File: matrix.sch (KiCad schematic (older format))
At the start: 134 parts, among them SW1 SW_Push, SW10 SW_Push, SW11 SW_Push, SW12 SW_Push, SW13 SW_Push, SW14 SW_Push, SW15 SW_Push, SW16 SW_Push, SW17 SW_Push, SW18 SW_Push, SW19 SW_Push, SW2 SW_Push, SW20 SW_Push, SW21 SW_Push, SW22 SW_Push, SW23 SW_Push, SW24 SW_Push, SW25 SW_Push, SW26 SW_Push, SW27 SW_Push, SW28 SW_Push, SW29 SW_Push, SW3 SW_Push, SW30 SW_Push, SW31 SW_Push, SW32 SW_Push, SW33 SW_Push, SW34 SW_Push, SW35 SW_Push, SW36 SW_Push, SW37 SW_Push, SW38 SW_Push, SW39 SW_Push, SW4 SW_Push, SW40 SW_Push, SW41 SW_Push, SW42 SW_Push, SW43 SW_Push, SW44 SW_Push, SW45 SW_Push, SW46 SW_Push, SW47 SW_Push, SW48 SW_Push, SW49 SW_Push, SW5 SW_Push, SW50 SW_Push, SW51 SW_Push, SW52 SW_Push, SW53 SW_Push, SW54 SW_Push, SW55 SW_Push, SW56 SW_Push, SW57 SW_Push, SW58 SW_Push, SW59 SW_Push, SW6 SW_Push, SW60 SW_Push, SW61 SW_Push, SW62 SW_Push, SW63 SW_Push, SW64 SW_Push, SW65 SW_Push, SW66 SW_Push, SW67 SW_Push, SW7 SW_Push, SW8 SW_Push, SW9 SW_Push

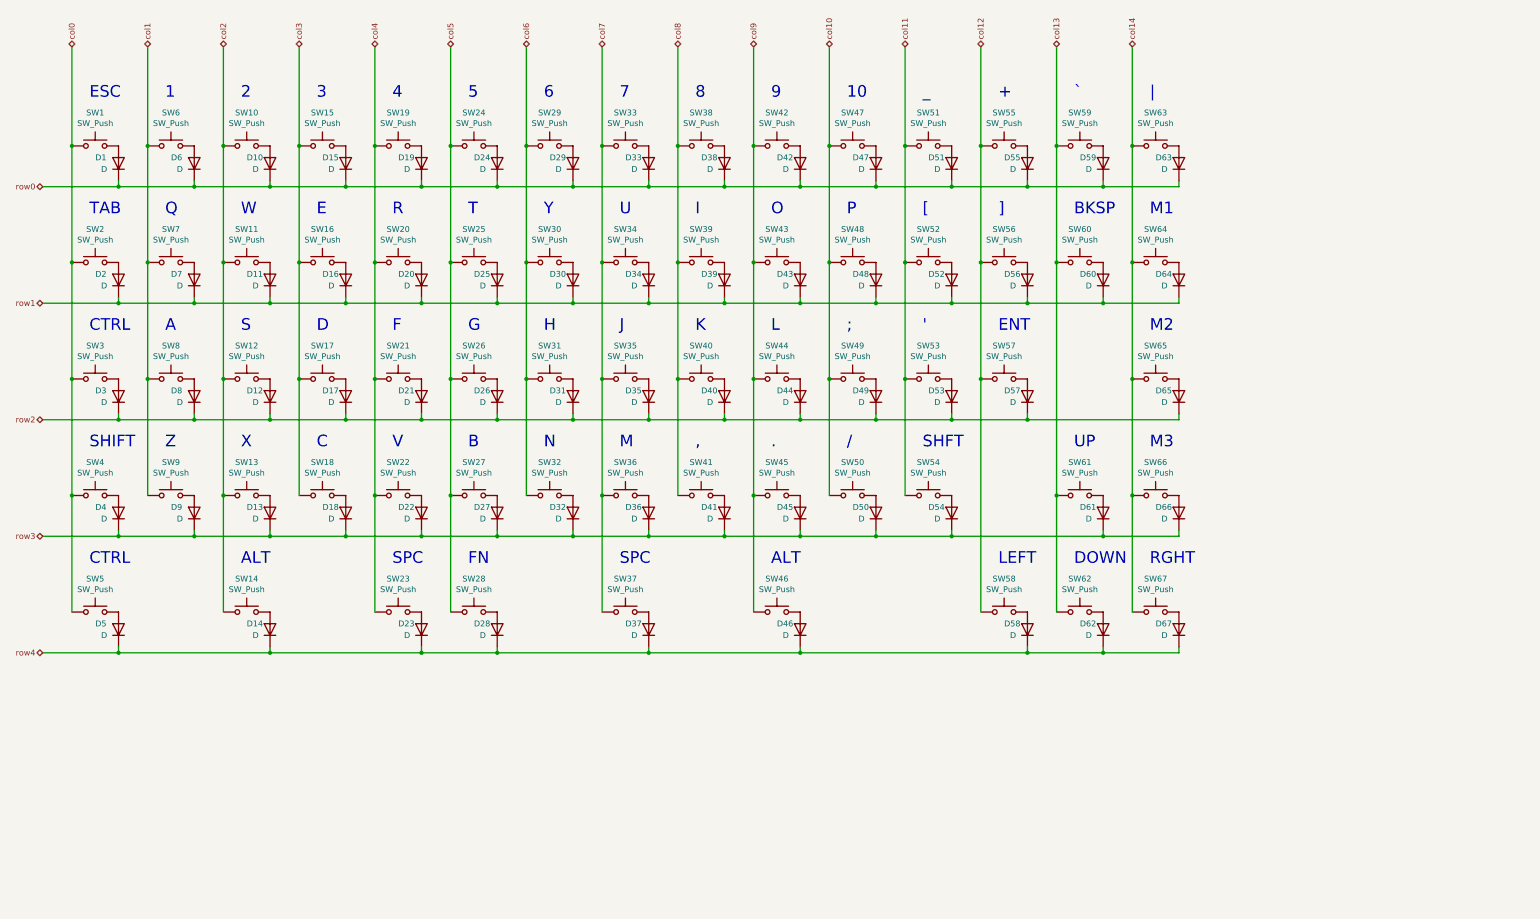
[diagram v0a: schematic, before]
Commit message: USB-C, hotswaps, ESD update, plates, so much
Added USB-C, updated case files, ESD rework, FR4 plates made, name change, hotswap sockets, route rework
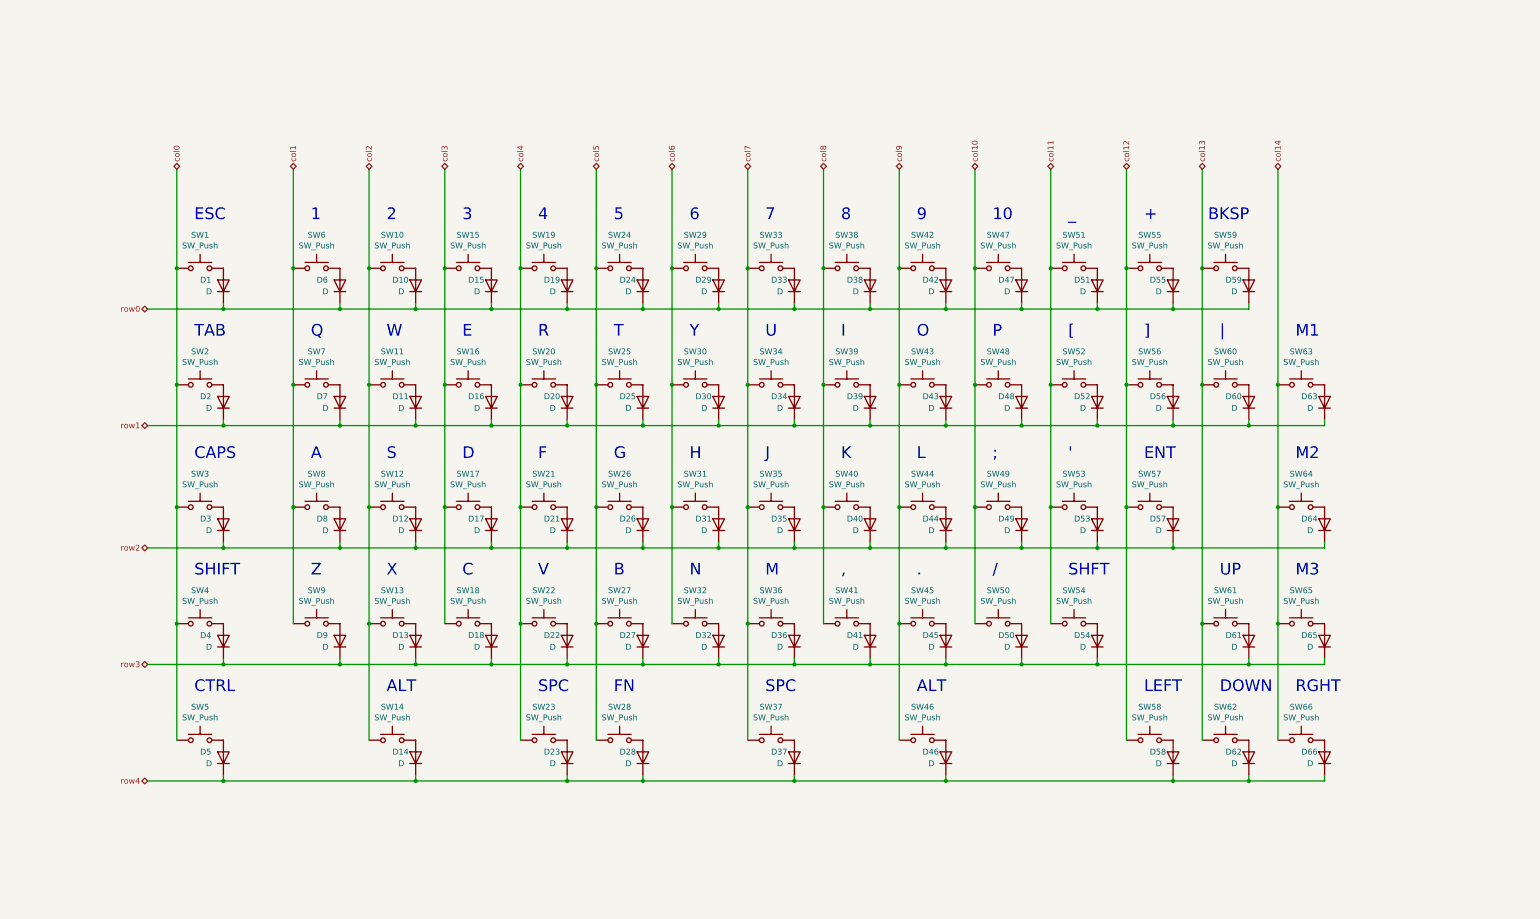
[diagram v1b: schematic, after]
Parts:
- removed D63: D, Diodes_SMD:D_SOD-123, symbol Device:D
- removed SW63: SW_Push, MX_Switch:SW_Cherry_MX_1.00u_PCB, symbol Switch:SW_Push
- D1, D10, D11, D12, D13, D14, D15, D16, D17, D18, D19, D2, D20, D21, D22, D23, D24, D25, D26, D27, D28, D29, D3, D30, D31, D32, D33, D34, D35, D36, D37, D38, D39, D4, D40, D41, D42, D43, D44, D45, D46, D47, D48, D49, D5, D50, D51, D52, D53, D54, D55, D56, D57, D58, D59, D6, D60, D61, D62, D7, D8, D9: footprint Diodes_SMD:D_SOD-123 -> Diode_SMD:D_SOD-123; LCSC (none) -> C81598
- D63: renamed from D64; footprint Diodes_SMD:D_SOD-123 -> Diode_SMD:D_SOD-123; LCSC (none) -> C81598
- D64: renamed from D65; footprint Diodes_SMD:D_SOD-123 -> Diode_SMD:D_SOD-123; LCSC (none) -> C81598
- D65: renamed from D66; footprint Diodes_SMD:D_SOD-123 -> Diode_SMD:D_SOD-123; LCSC (none) -> C81598
- D66: renamed from D67; footprint Diodes_SMD:D_SOD-123 -> Diode_SMD:D_SOD-123; LCSC (none) -> C81598
- SW1, SW10, SW11, SW12, SW13, SW15, SW16, SW17, SW18, SW19, SW20, SW21, SW22, SW24, SW25, SW26, SW27, SW28, SW29, SW30, SW31, SW32, SW33, SW34, SW35, SW36, SW38, SW39, SW40, SW41, SW42, SW43, SW44, SW45, SW47, SW48, SW49, SW50, SW51, SW52, SW53, SW55, SW56, SW58, SW6, SW61, SW62, SW7, SW8, SW9: footprint MX_Switch:SW_Cherry_MX_1.00u_PCB -> arisutea:SW_Hotswap_Kailh_1.00u
- SW14, SW46: footprint MX_Switch:SW_Cherry_MX_1.50u_PCB -> arisutea:SW_Hotswap_Kailh_1.00u
- SW2, SW5, SW60: footprint MX_Switch:SW_Cherry_MX_1.50u_PCB -> arisutea:SW_Hotswap_Kailh_1.50u
- SW23: footprint MX_Switch:SW_Cherry_MX_2.00u_PCB_ReversedStabilizers -> arisutea:SW_Hotswap_Kailh_2.00u_RevStab
- SW3, SW54: footprint MX_Switch:SW_Cherry_MX_1.75u_PCB -> arisutea:SW_Hotswap_Kailh_1.75u
- SW37: footprint MX_Switch:SW_Cherry_MX_2.75u_PCB_ReversedStabilizers -> arisutea:SW_Hotswap_Kailh_2.75u_RevStab
- SW4: footprint MX_Switch:SW_Cherry_MX_2.25u_PCB -> arisutea:SW_Hotswap_Kailh_2.25u
- SW57: footprint MX_Switch:SW_Cherry_MX_2.25u_PCB_ReversedStabilizers -> arisutea:SW_Hotswap_Kailh_2.25u_RevStab
- SW59: footprint MX_Switch:SW_Cherry_MX_1.00u_PCB -> arisutea:SW_Hotswap_Kailh_2.00u
- SW63: renamed from SW64; footprint MX_Switch:SW_Cherry_MX_1.00u_PCB -> arisutea:SW_Hotswap_Kailh_1.00u
- SW64: renamed from SW65; footprint MX_Switch:SW_Cherry_MX_1.00u_PCB -> arisutea:SW_Hotswap_Kailh_1.00u
- SW65: renamed from SW66; footprint MX_Switch:SW_Cherry_MX_1.00u_PCB -> arisutea:SW_Hotswap_Kailh_1.00u
- SW66: renamed from SW67; footprint MX_Switch:SW_Cherry_MX_1.00u_PCB -> arisutea:SW_Hotswap_Kailh_1.00u
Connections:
- net col0: now also SW1.2, SW2.2, SW3.2, SW4.2, SW5.2; no longer SW1.1, SW2.1, SW3.1, SW4.1, SW5.1
- net col1: now also SW6.2, SW7.2, SW8.2, SW9.2; no longer SW6.1, SW7.1, SW8.1, SW9.1
- net col10: now also SW47.2, SW48.2, SW49.2, SW50.2; no longer SW47.1, SW48.1, SW49.1, SW50.1
- net col11: now also SW51.2, SW52.2, SW53.2, SW54.2; no longer SW51.1, SW52.1, SW53.1, SW54.1
- net col12: now also SW55.2, SW56.2, SW57.2, SW58.2; no longer SW55.1, SW56.1, SW57.1, SW58.1
- net col13: now also SW59.2, SW60.2, SW61.2, SW62.2; no longer SW59.1, SW60.1, SW61.1, SW62.1
- net col14: now also SW63.2, SW64.2, SW65.2, SW66.2; no longer SW63.1, SW64.1, SW65.1, SW66.1
- net col2: now also SW10.2, SW11.2, SW12.2, SW13.2, SW14.2; no longer SW10.1, SW11.1, SW12.1, SW13.1, SW14.1
- net col3: now also SW15.2, SW16.2, SW17.2, SW18.2; no longer SW15.1, SW16.1, SW17.1, SW18.1
- net col4: now also SW19.2, SW20.2, SW21.2, SW22.2, SW23.2; no longer SW19.1, SW20.1, SW21.1, SW22.1, SW23.1
- net col5: now also SW24.2, SW25.2, SW26.2, SW27.2, SW28.2; no longer SW24.1, SW25.1, SW26.1, SW27.1, SW28.1
- net col6: now also SW29.2, SW30.2, SW31.2, SW32.2; no longer SW29.1, SW30.1, SW31.1, SW32.1
- net col7: now also SW33.2, SW34.2, SW35.2, SW36.2, SW37.2; no longer SW33.1, SW34.1, SW35.1, SW36.1, SW37.1
- net col8: now also SW38.2, SW39.2, SW40.2, SW41.2; no longer SW38.1, SW39.1, SW40.1, SW41.1
- net col9: now also SW42.2, SW43.2, SW44.2, SW45.2, SW46.2; no longer SW42.1, SW43.1, SW44.1, SW45.1, SW46.1
- net at D1.2 (A): now also SW1.1; no longer SW1.2
- net at D6.2 (A): now also SW6.1; no longer SW6.2
- net at D2.2 (A): now also SW2.1; no longer SW2.2
- net at D7.2 (A): now also SW7.1; no longer SW7.2
- net at D3.2 (A): now also SW3.1; no longer SW3.2
- net at D4.2 (A): now also SW4.1; no longer SW4.2
- net at D5.2 (A): now also SW5.1; no longer SW5.2
- net at D8.2 (A): now also SW8.1; no longer SW8.2
- net at D9.2 (A): now also SW9.1; no longer SW9.2
- net at D10.2 (A): now also SW10.1; no longer SW10.2
- net at D11.2 (A): now also SW11.1; no longer SW11.2
- net at D12.2 (A): now also SW12.1; no longer SW12.2
- net at D13.2 (A): now also SW13.1; no longer SW13.2
- net at D14.2 (A): now also SW14.1; no longer SW14.2
- net at D15.2 (A): now also SW15.1; no longer SW15.2
- net at D16.2 (A): now also SW16.1; no longer SW16.2
- net at D17.2 (A): now also SW17.1; no longer SW17.2
- net at D18.2 (A): now also SW18.1; no longer SW18.2
- net at D19.2 (A): now also SW19.1; no longer SW19.2
- net at D20.2 (A): now also SW20.1; no longer SW20.2
- net at D21.2 (A): now also SW21.1; no longer SW21.2
- net at D22.2 (A): now also SW22.1; no longer SW22.2
- net at D23.2 (A): now also SW23.1; no longer SW23.2
- net at D24.2 (A): now also SW24.1; no longer SW24.2
- net at D25.2 (A): now also SW25.1; no longer SW25.2
- net at D26.2 (A): now also SW26.1; no longer SW26.2
- net at D27.2 (A): now also SW27.1; no longer SW27.2
- net at D28.2 (A): now also SW28.1; no longer SW28.2
- net at D29.2 (A): now also SW29.1; no longer SW29.2
- net at D30.2 (A): now also SW30.1; no longer SW30.2
- net at D31.2 (A): now also SW31.1; no longer SW31.2
- net at D32.2 (A): now also SW32.1; no longer SW32.2
- net at D33.2 (A): now also SW33.1; no longer SW33.2
- net at D34.2 (A): now also SW34.1; no longer SW34.2
- net at D35.2 (A): now also SW35.1; no longer SW35.2
- net at D36.2 (A): now also SW36.1; no longer SW36.2
- net at D37.2 (A): now also SW37.1; no longer SW37.2
- net at D38.2 (A): now also SW38.1; no longer SW38.2
- net at D39.2 (A): now also SW39.1; no longer SW39.2
- net at D40.2 (A): now also SW40.1; no longer SW40.2
- net at D41.2 (A): now also SW41.1; no longer SW41.2
- net at D42.2 (A): now also SW42.1; no longer SW42.2
- net at D43.2 (A): now also SW43.1; no longer SW43.2
- net at D44.2 (A): now also SW44.1; no longer SW44.2
- net at D45.2 (A): now also SW45.1; no longer SW45.2
- net at D46.2 (A): now also SW46.1; no longer SW46.2
- net at D47.2 (A): now also SW47.1; no longer SW47.2
- net at D48.2 (A): now also SW48.1; no longer SW48.2
- net at D49.2 (A): now also SW49.1; no longer SW49.2
- net at D50.2 (A): now also SW50.1; no longer SW50.2
- net at D51.2 (A): now also SW51.1; no longer SW51.2
- net at D52.2 (A): now also SW52.1; no longer SW52.2
- net at D53.2 (A): now also SW53.1; no longer SW53.2
- net at D54.2 (A): now also SW54.1; no longer SW54.2
- net at D55.2 (A): now also SW55.1; no longer SW55.2
- net at D56.2 (A): now also SW56.1; no longer SW56.2
- net at D57.2 (A): now also SW57.1; no longer SW57.2
- net at D58.2 (A): now also SW58.1; no longer SW58.2
- net at D59.2 (A): now also SW59.1; no longer SW59.2
- net at D60.2 (A): now also SW60.1; no longer SW60.2
- net at D61.2 (A): now also SW61.1; no longer SW61.2
- net at D62.2 (A): now also SW62.1; no longer SW62.2
- net at D63.2 (A): now also SW63.1; no longer SW63.2
- net at D64.2 (A): now also SW64.1; no longer SW64.2
- net at D65.2 (A): now also SW65.1; no longer SW65.2
- net at D66.2 (A): now also SW66.1; no longer SW66.2
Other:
- note added: "CAPS"
- note removed: "`"
- moved on the sheet: D1, D10, D11, D12, D13, D14, D15, D16, D17, D18, D19, D2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

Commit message: library, silkscreen and gerber update
I moved all the footprints into a single library so that if folks don't have the particular lib they won't have to go and search for it or try to replace. Silkscreen was updated again to show clearer positioning of components and gerbers updated to most recent. Version number isn't changing as no big updates were made.
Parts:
- D1, D10, D11, D12, D13, D14, D15, D16, D17, D18, D19, D2, D20, D21, D22, D23, D24, D25, D26, D27, D28, D29, D3, D30, D31, D32, D33, D34, D35, D36, D37, D38, D39, D4, D40, D41, D42, D43, D44, D45, D46, D47, D48, D49, D5, D50, D51, D52, D53, D54, D55, D56, D57, D58, D59, D6, D60, D61, D62, D63, D64, D65, D66, D7, D8, D9: footprint Diode_SMD:D_SOD-123 -> arisutea:D_SOD-123

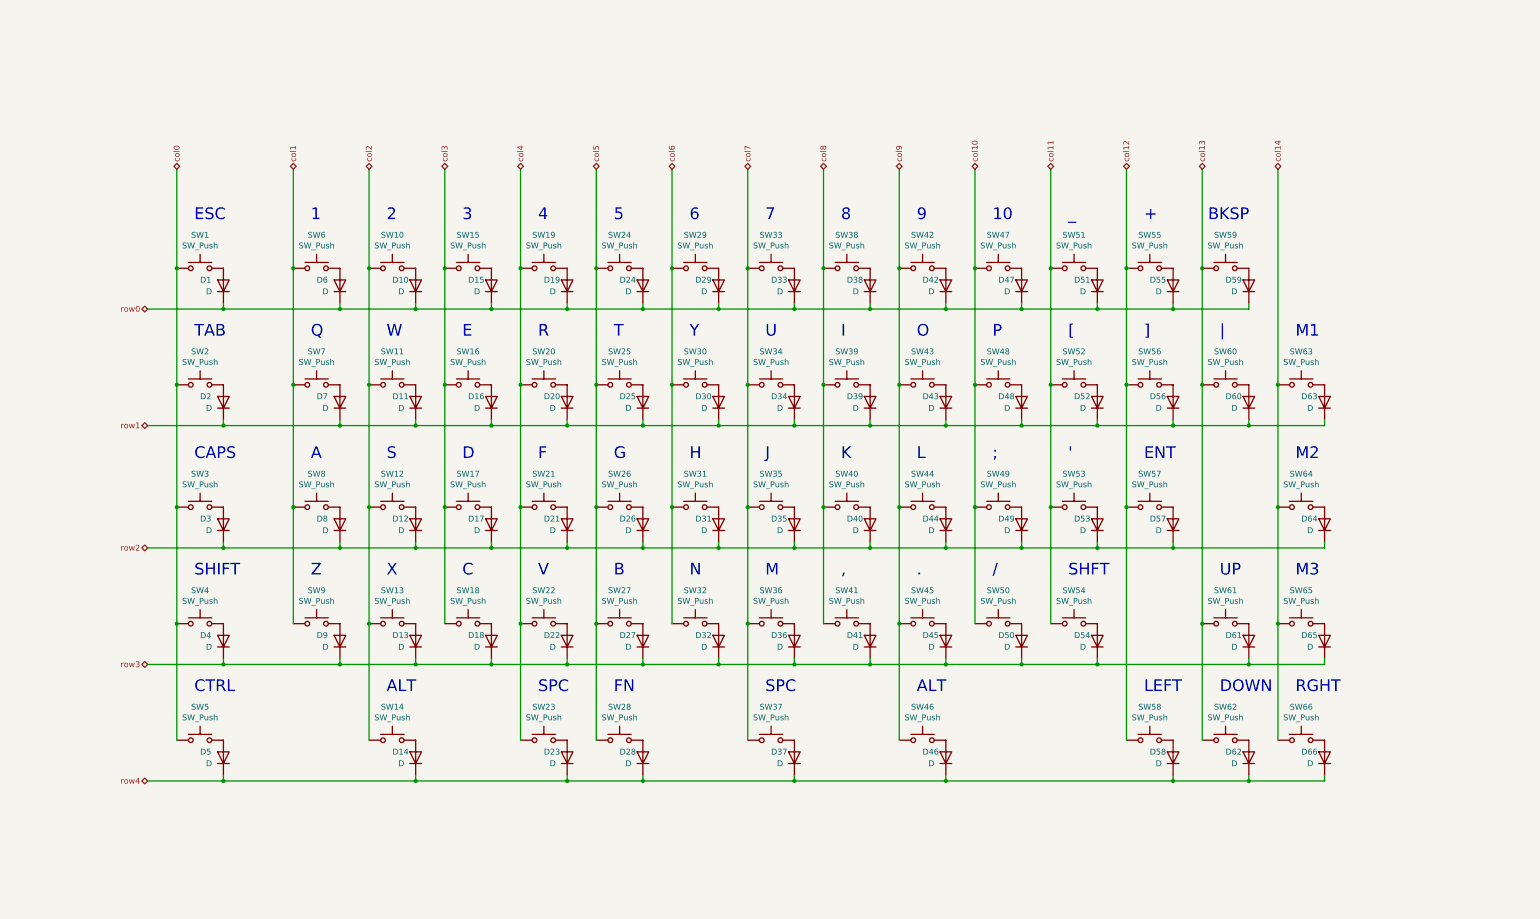
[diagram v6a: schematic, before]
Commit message: added LED strip and indicator support, new cases for indicators
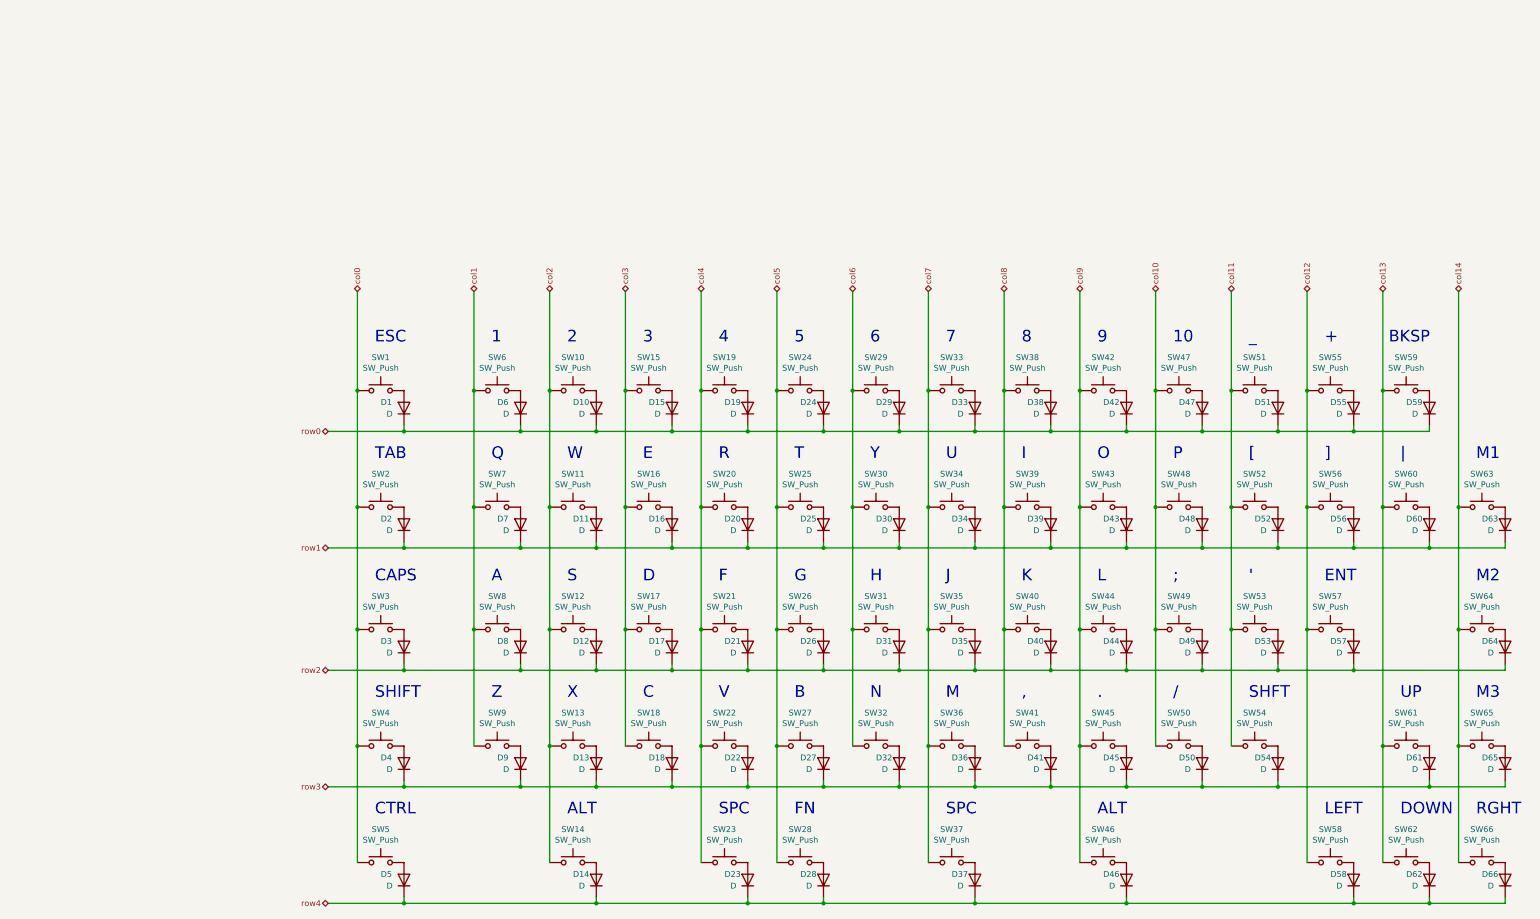
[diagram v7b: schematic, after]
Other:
- moved on the sheet: D1, D10, D11, D12, D13, D14, D15, D16, D17, D18, D19, D2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
